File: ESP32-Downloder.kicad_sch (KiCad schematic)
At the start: 21 parts, among them J1 USB_C_Receptacle_USB2.0_16P, J2 ESP32_DOWNLOAD_CON, Q1 BSS138, Q2 BSS138, SW1 RESET, SW2 FLASH, U1 CH340K, U2 AMS1117-3.3

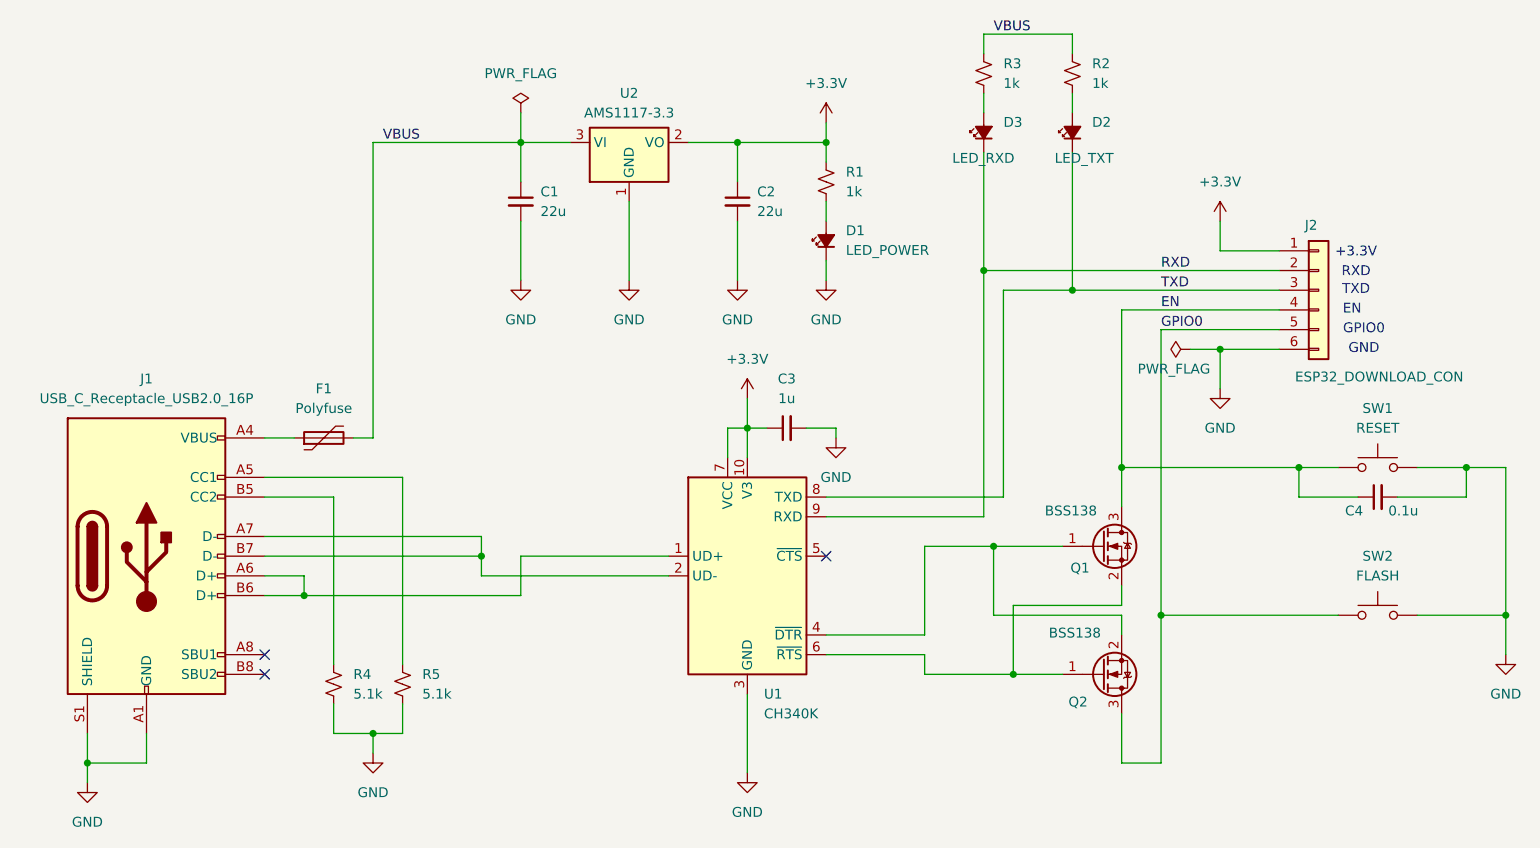
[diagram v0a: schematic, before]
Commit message: README追加、ガーバーデータ出力
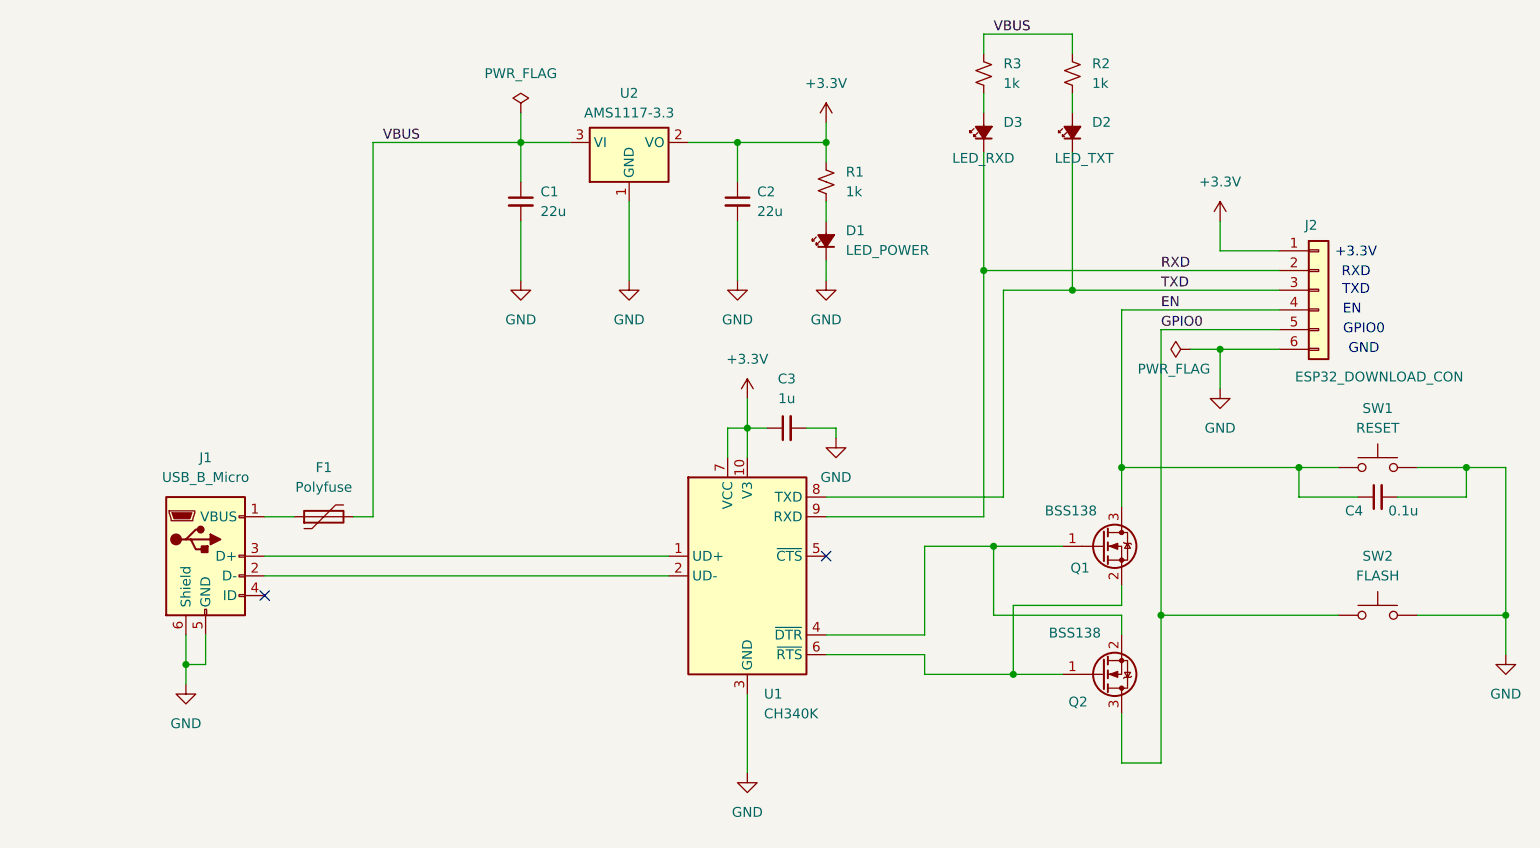
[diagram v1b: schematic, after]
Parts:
- removed J1: USB_C_Receptacle_USB2.0_16P, Connector_USB:USB_C_Receptacle_XKB_U262-16XN-4BVC11, symbol Connector:USB_C_Receptacle_USB2.0_16P
- removed R4, R5: 5.1k, Resistor_SMD:R_0603_1608Metric_Pad0.98x0.95mm_HandSolder, symbol Device:R_Small_US
- added J1: USB_B_Micro, Connector_USB:USB_Micro-B_Molex-105017-0001, symbol Connector:USB_B_Micro
- J2: footprint Connector_PinHeader_2.54mm:PinHeader_1x06_P2.54mm_Horizontal -> Connector_PinSocket_2.54mm:PinSocket_1x06_P2.54mm_Horizontal
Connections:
- net GND: now also J1.5 (GND), J1.6 (Shield)
- net at F1.1: now also J1.1 (VBUS)
- net at U1.1 (UD+): now also J1.3 (D+)
- net at U1.2 (UD-): now also J1.2 (D-)
- no-connect marks 3 -> 2
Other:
- moved on the sheet: F1
